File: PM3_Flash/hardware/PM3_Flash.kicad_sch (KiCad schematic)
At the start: 4 parts, among them J1 Conn_01x02, J2 Conn_01x04, U1 W25Qxx

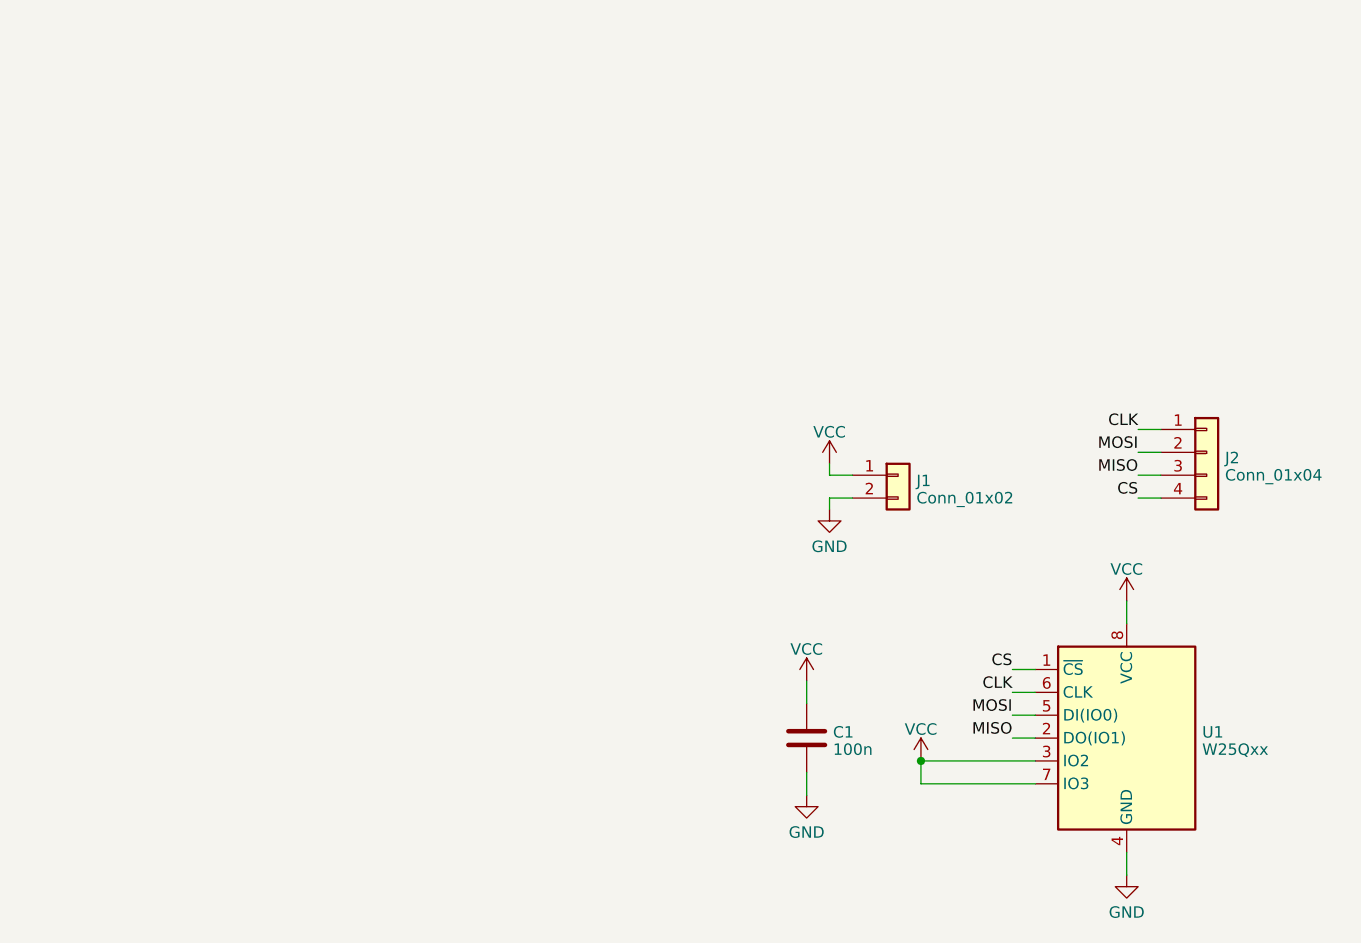
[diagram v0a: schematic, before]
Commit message: Add schematic pdf
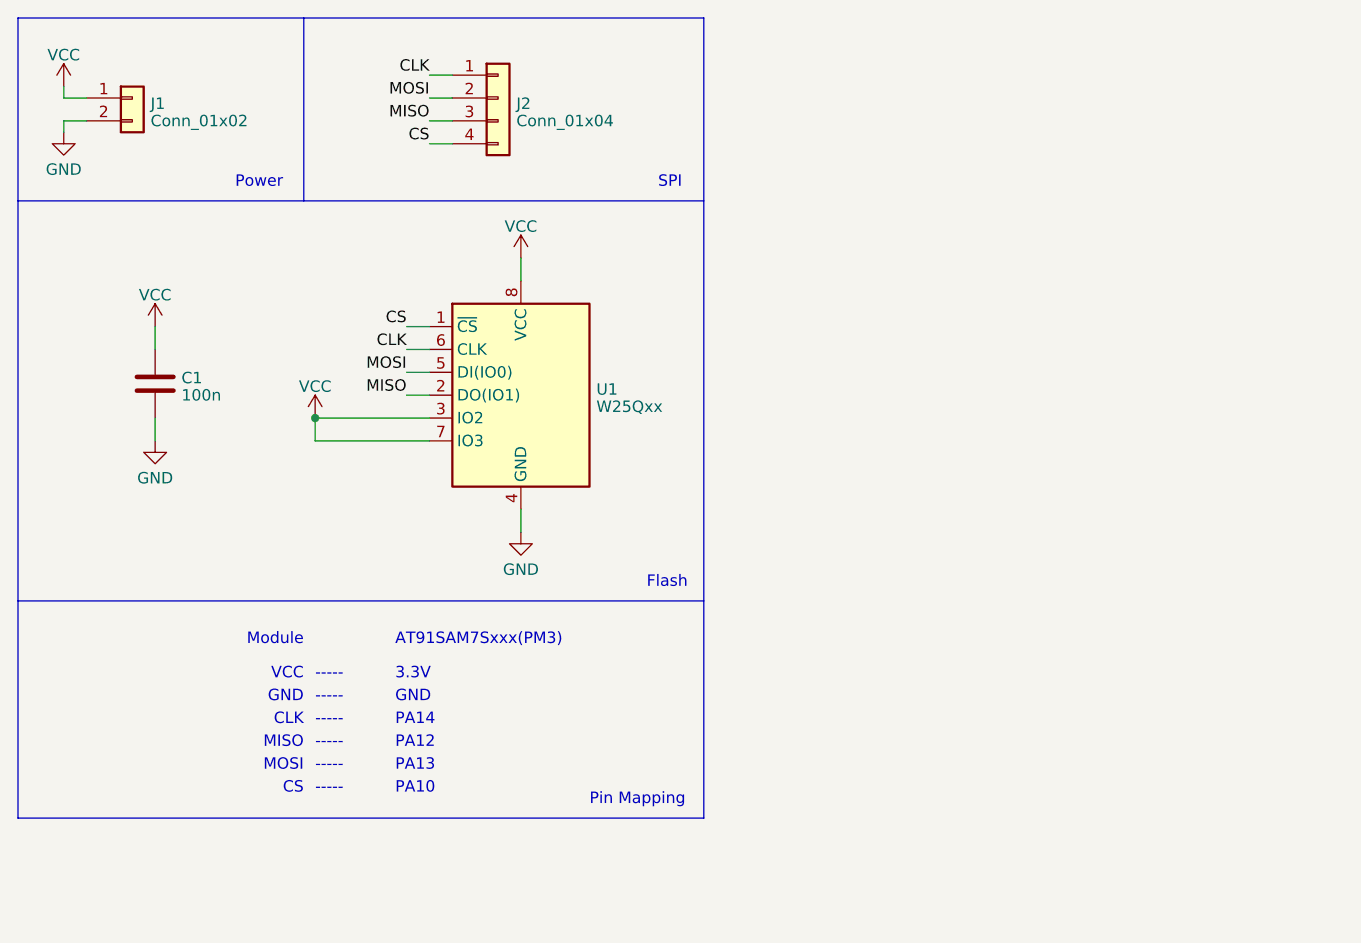
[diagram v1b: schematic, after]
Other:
- note added: "-----"
- note added: "3.3V"
- note added: "AT91SAM7Sxxx(PM3)"
- note added: "CLK"
- note added: "CS"
- note added: "Flash"
- note added: "GND"
- note added: "MISO"
- note added: "MOSI"
- note added: "Module"
- note added: "PA10"
- note added: "PA12"
- note added: "PA13"
- note added: "PA14"
- note added: "Pin Mapping"
- note added: "Power"
- note added: "SPI"
- note added: "VCC"
- moved on the sheet: C1, J1, J2, U1
